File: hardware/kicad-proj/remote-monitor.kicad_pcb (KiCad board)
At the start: 2 copper layers, 80 x 80 mm, 30 parts, among them J1 Screw_Terminal_01x10, J2 USB_A, U1 OKI-78SR-5, U2 OKI-78SR-5

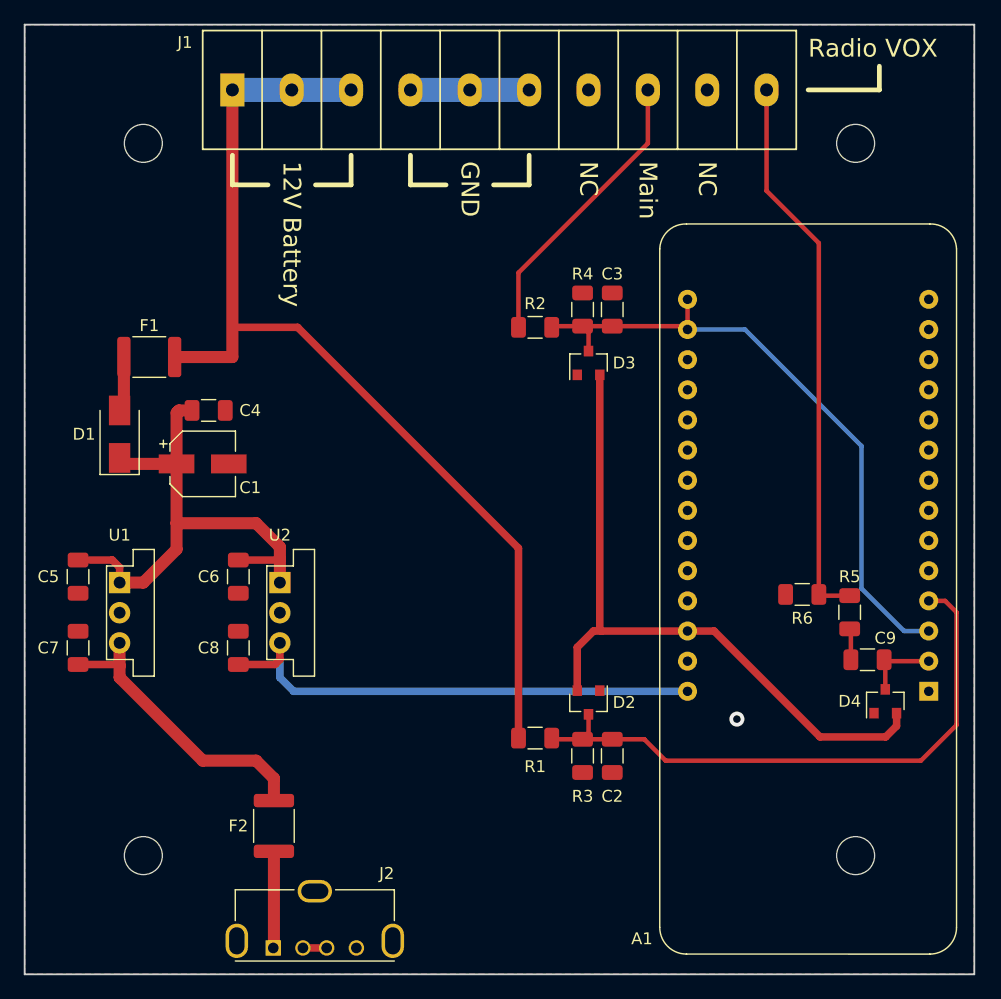
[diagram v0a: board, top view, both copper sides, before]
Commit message: updated pcb dimensions and mounting holes for different enclosure
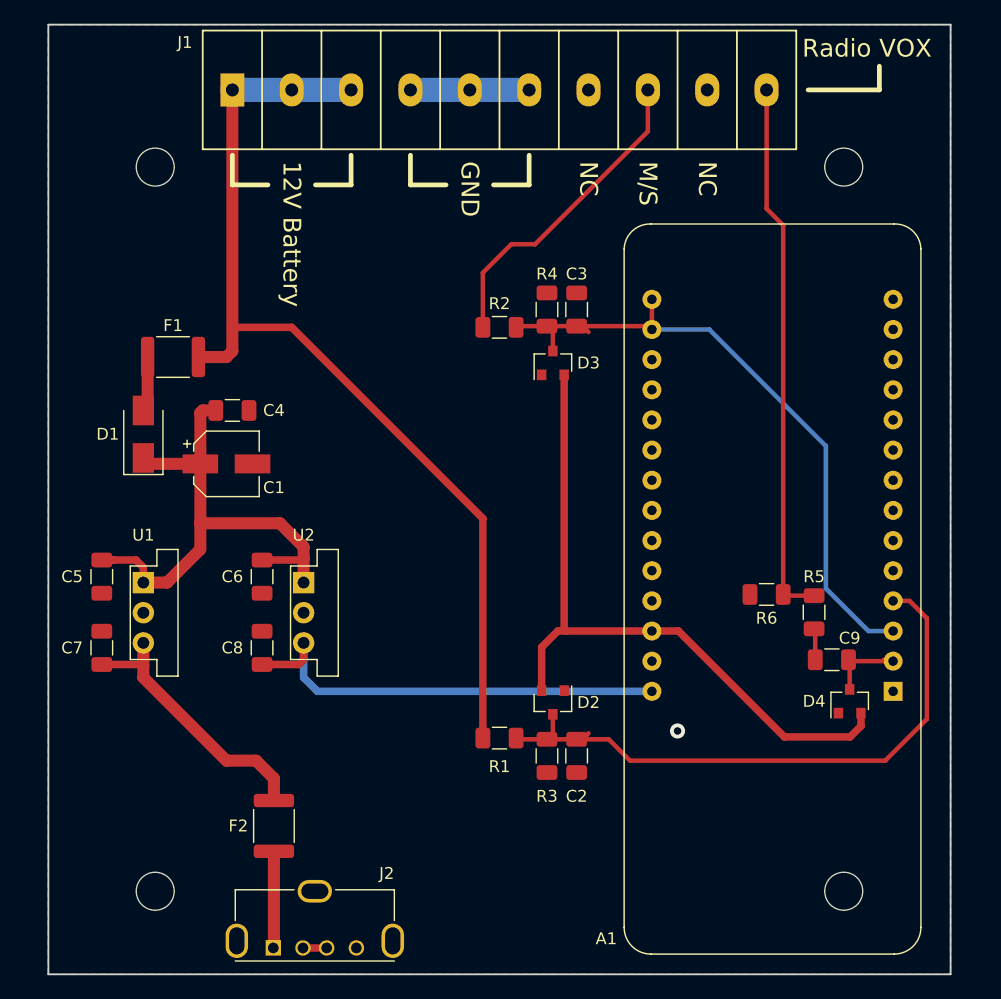
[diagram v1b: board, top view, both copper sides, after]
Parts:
- moved REF** 3.16 mm to (164.0, 118.0)
- moved REF** 3.16 mm to (106.0, 118.0)
- moved A1 3.00 mm to (158.0, 91.0)
- moved C2 3.00 mm to (141.5, 106.6)
- moved C3 3.00 mm to (141.5, 69.0)
- moved C9 3.00 mm to (163.0, 98.5)
- moved D2 3.00 mm to (139.5, 102.1)
- moved D3 3.00 mm to (139.5, 73.5)
- moved D4 3.00 mm to (164.5, 102.0)
- moved R1 3.00 mm to (135.0, 105.1)
- moved R2 3.00 mm to (135.0, 70.5)
- moved R3 3.00 mm to (139.0, 106.6)
- moved R4 3.00 mm to (139.0, 69.0)
- moved R5 3.00 mm to (161.5, 94.5)
- moved R6 3.00 mm to (157.5, 93.0)
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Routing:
- net +5V: track 42.8 -> 37.8 mm
- net Net-(F1-Pad2): track 85.2 -> 81.3 mm
- net Net-(J1-Pad8): track 24.5 -> 26.9 mm
- net Net-(C7-Pad1): track 24.8 -> 22.7 mm
- net /Radio_VOX: track 47.0 -> 45.7 mm
- net Net-(C1-Pad1): track 45.0 -> 44.2 mm
- net Net-(D1-Pad2): track 4.65 -> 4.14 mm
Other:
- board size 80 x 80 mm -> 76 x 80 mm
- board text added: "M/S"
- board text removed: "Main"

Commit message: updated hardware designs
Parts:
- removed REF** (x4): MountingHole_3.2mm_M3, MountingHole:MountingHole_3.2mm_M3
- added C10: 4.7uf, Capacitor_SMD:C_1206_3216Metric, F.Cu at (152.5, 64.5)
- added C11: 4.7uf, Capacitor_SMD:C_1206_3216Metric, F.Cu at (135.0, 65.0)
- added C12: 470uf, Capacitor_SMD:CP_Elec_8x10.5, F.Cu at (126.0, 67.5)
- added C13: 100nf, Capacitor_SMD:C_1206_3216Metric, F.Cu at (126.0, 98.0)
- added L1: 1mH, Inductor_SMD:L_6.3x6.3_H3, F.Cu at (132.5, 77.0)
- added U3: NCP51460, Package_TO_SOT_SMD:SOT-23, F.Cu at (153.5, 82.5)
- C1: value 10uF -> 10uf
- C3: value 100nf -> 1nf
- C7, C8: value C -> 1uf
- F1: value 1A -> 0.5A
- J1: value Screw_Terminal_01x10 -> Screw Terminal
- R4: value 10k -> 100k
- R6: value 1K -> 100k
- moved R6 20.2 mm to (140.0, 83.0)
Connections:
- A1 pad 1: Net-(A1-Pad1) -> /AREF
- A1 pad 15: /Mains_Sensor -> Net-(A1-Pad15)
- A1 pad 16: /Mains_Sensor -> Net-(A1-Pad16)
- C8 pad 1: +5V -> Net-(C8-Pad1)
- D3 pad 2: +3V3 -> /AREF
- J1 pad 10: /Radio_VOX -> /Radio_Sig
- J1 pad 8: Net-(J1-Pad8) -> Net-(C11-Pad1)
- J1 pad 9: Net-(J1-Pad9) -> /Radio_GND
- R2 pad 2: Net-(J1-Pad8) -> Net-(C11-Pad2)
- R5 pad 2: /Radio_VOX -> /Radio_Sig
- R6 pad 1: /Radio_VOX -> /Mains_Sensor
- R6 pad 2: GND -> /AREF
- U2 pad 3: +5V -> Net-(C8-Pad1)
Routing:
- net /Radio_VOX: track 45.7 -> 0.00 mm
- net /Radio_Sig: track 0.00 -> 45.7 mm
- net Net-(J1-Pad8): track 26.9 -> 0.00 mm
- net +3V3: track 57.9 -> 36.3 mm
- net Net-(C11-Pad1): track 0.00 -> 16.9 mm
- net /Mains_Sensor: track 54.1 -> 53.4 mm
